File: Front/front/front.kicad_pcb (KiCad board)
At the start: 2 copper layers, 28.5 x 51.8 mm, 13 parts, among them J1 JST PH 1mm 4-Pin Connector, J2 Conn_01x10_Male, SW1 SW_Push, U1 L293D

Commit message: Version 0.1.2 - First draft of front PCB complete
Signed-off-by: ray33ee <30669752+ray33ee@users.noreply.github.com>
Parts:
- added C2: 100nF, Capacitor_SMD:C_1206_3216Metric_Pad1.33x1.80mm_HandSolder, F.Cu at (199.5, 126.2)
- J1: value JST PH 1mm 4-Pin Connector -> JST 1mm Connector
- moved R4 7.56 mm to (195.7, 97.9)
- moved R3 6.36 mm to (216.9, 85.1)
- moved R2 3.82 mm to (216.9, 89.5)
- moved U1 3.32 mm to (202.3, 110.0)
- moved JP1 1.95 mm to (200.8, 100.3)
- moved R1 0.89 mm to (195.6, 87.6)
- moved D1 0.78 mm to (207.7, 85.4)
- moved D2 0.62 mm to (199.9, 85.4)
- moved J2 0.33 mm to (194.6, 81.9)
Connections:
- net Net-(D1-Pad1) renamed /Motor_Supply_Pre
- net Net-(J1-Pad1) renamed /JST_PIN_1
- net Net-(J1-Pad2) renamed /JST_PIN_2
- net Net-(J1-Pad3) renamed /JST_PIN_3
- net Net-(J1-Pad4) renamed /JST_PIN_4
- J2 pad 5: /Enable -> /Enable_Controlled
- JP1 pad 1: /Enable -> /Enable_High
- JP1 pad 2: Net-(JP1-Pad2) -> /Enable
- JP1 pad 3: Net-(JP1-Pad3) -> /Enable_Controlled
- R4 pad 2: Net-(JP1-Pad3) -> /Enable_High
- U1 pad 1: Net-(JP1-Pad2) -> /Enable
- U1 pad 9: Net-(JP1-Pad2) -> /Enable
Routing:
- net +5V: track 0.00 -> 77.6 mm, vias 0 -> 6
- net GND: track 0.00 -> 70.1 mm, vias 0 -> 9
- net /Motor_Supply_Pre: track 0.00 -> 67.8 mm, vias 0 -> 3
- net /PushButton1: track 0.00 -> 64.9 mm, vias 0 -> 1
- net /Coil_A2: track 0.00 -> 61.8 mm, vias 0 -> 1
- net /Coil_B1: track 0.00 -> 50.2 mm
- net /Enable: track 0.00 -> 48.8 mm, vias 0 -> 2
- net /Coil_A1: track 0.00 -> 46.8 mm, vias 0 -> 2
- net /JST_PIN_2: track 0.00 -> 41.0 mm, vias 0 -> 2
- net /Coil_B2: track 0.00 -> 38.4 mm, vias 0 -> 2
- net /JST_PIN_3: track 0.00 -> 33.5 mm, vias 0 -> 2
- net /JST_PIN_4: track 0.00 -> 32.3 mm, vias 0 -> 2
- net /JST_PIN_1: track 0.00 -> 27.9 mm, vias 0 -> 2
- net /Enable_Controlled: track 0.00 -> 19.6 mm
- net /Diff_P1: track 0.00 -> 16.8 mm
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- added copper zone on B.Cu, net GND
- added copper zone on F.Cu, net GND
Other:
- net class Default: clearance 0.2 -> 0.127; trace_width 0.25 -> 0.15; via_dia 0.8 -> 0.4; via_drill 0.4 -> 0.2
- net class High Current added: clearance 0.15, trace_width 0.6, via_dia 0.6, via_drill 0.3
- rule trace_clearance: 0.2 -> 0.127
- rule trace_min: 0.2 -> 0.127
- rule via_min_drill: 0.3 -> 0.2

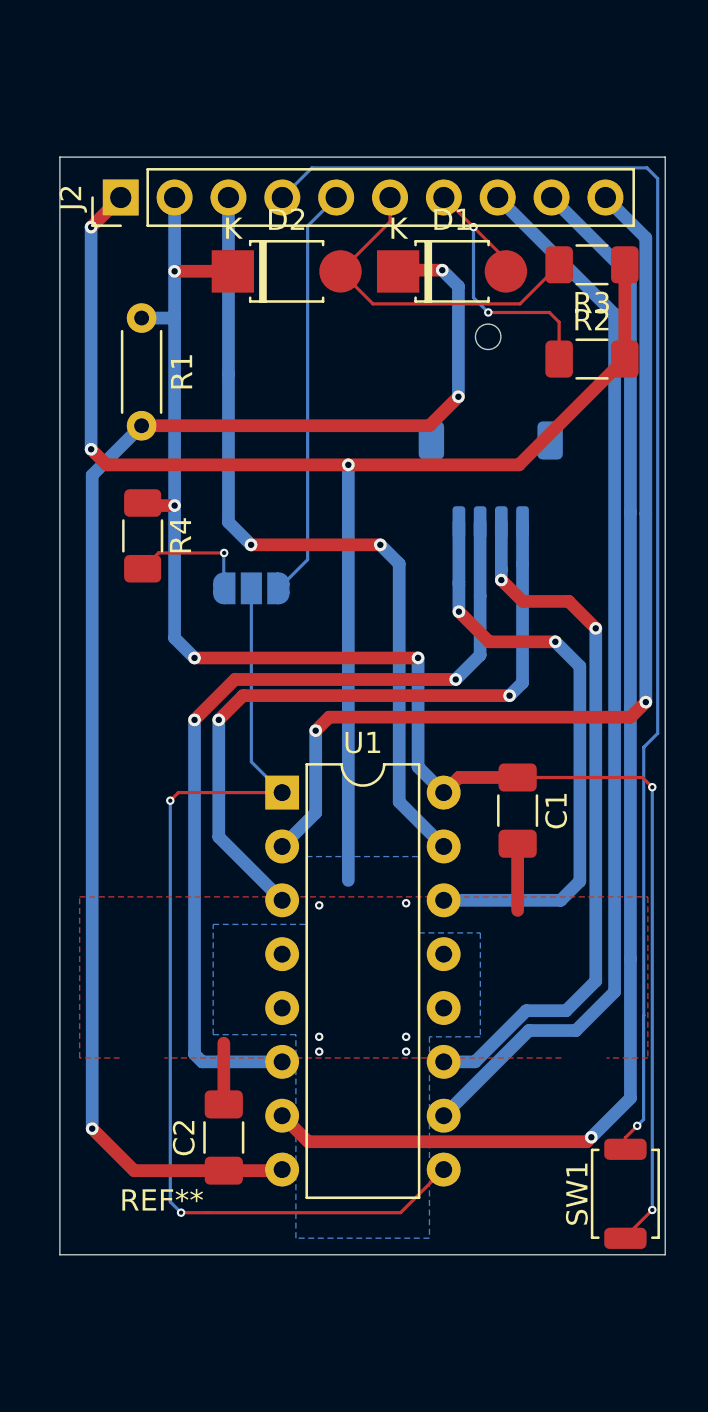
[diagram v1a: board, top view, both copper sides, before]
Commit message: Version 0.1.3 - Various changes, see changelog
Signed-off-by: ray33ee <30669752+ray33ee@users.noreply.github.com>
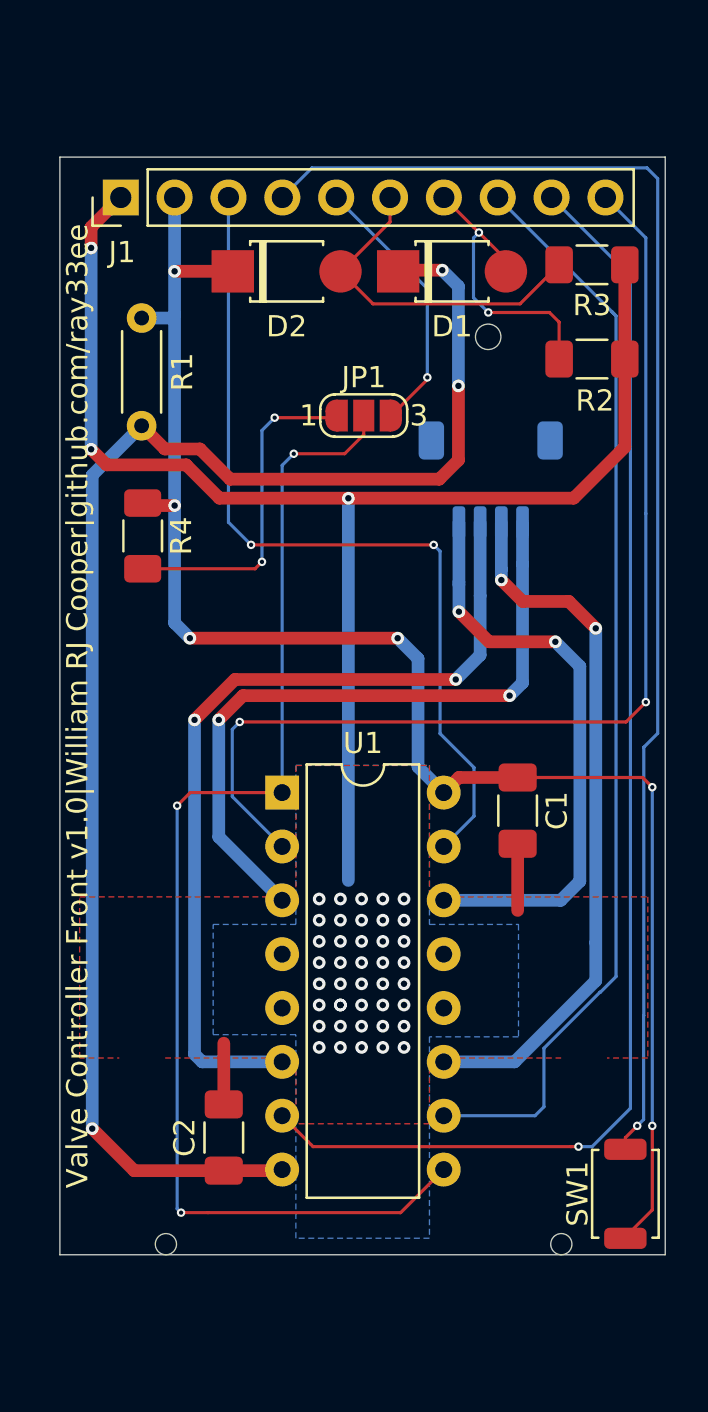
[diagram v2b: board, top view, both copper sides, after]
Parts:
- JP1: moved to F.Cu
- moved JP1 9.72 mm to (206.1, 92.2)
- renumbered J2 to J1, J1 to J2
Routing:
- net /Enable: track 48.8 -> 58.7 mm, vias 2 -> 3
- net /Enable_High: track 7.35 -> 16.5 mm, vias 1 -> 2
- net /Enable_Controlled: track 19.6 -> 12.8 mm, vias 0 -> 1
- net /Coil_A1: track 46.8 -> 51.1 mm
- net /Motor_Supply_Pre: track 67.8 -> 71.6 mm
- net /Coil_B2: track 38.4 -> 41.0 mm
- net GND: track 70.1 -> 72.2 mm, vias 9 -> 44
- net /Coil_B1: track 50.2 -> 51.7 mm
- net /Diff_P2: track 15.8 -> 16.3 mm
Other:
- board text added: "JLCJLCJLCJLC"
- board text added: "Valve Controller Front v1.0|William RJ Cooper|github.com/ray33ee"
